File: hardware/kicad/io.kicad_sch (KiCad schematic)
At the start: 0 parts

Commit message: kicad+docs: v0.19 - IO sub-sheet populated (J9 Qwiic + J10 native-USB recovery DNP)
Closes review Mi4 ("IO sub-sheet still empty"). Implements both connectors
listed in CLAUDE.md as "tentative" since v0.1:

J9 - Qwiic / Stemma QT expansion (always populated)
  Stock JST_SH SM04B-SRSS-TB 4-pin horizontal SMD socket on cutout C5.
  Cable mouth faces the chord so the cable plugs in from outside the
  case. Pinout: GND / +3.3V / SDA / SCL — taps the shared I2C bus
  (SEN66 + NT3H1101 + Qwiic chain). I2C_SDA / I2C_SCL hier labels
  match the MCU exports.

J10 - Native-USB recovery header (DNP)
  Stock 6-pin 2.54 mm vertical THT pin header on cutout C3. Pads
  only — solder a header for emergency reflashing if both DevKitM-1
  on-module USB-C ports are damaged. Pinout (chord side → PCB
  interior): GND / +3V3 / USB_DM (GPIO 12) / USB_DP (GPIO 13) /
  EN (chip reset) / BOOT (GPIO 9 strap).

Cutout C4 reserved as v2 expansion placeholder (no connector).

Key plumbing changes:
  - GPIO 12 / GPIO 13 moved from ESP32C6_DEVKITM1_NC_PINS to
    ESP32C6_DEVKITM1_SIGNAL_PIN as USB_DM / USB_DP. MCU sheet now
    wires U3.28 / U3.29 east to hier labels.
  - EN / BOOT migrated from MCU sub-sheet local labels to hier
    labels so the same nets reach the IO sheet's J10.5 / J10.6.
    J2_PIN_MAP[5] "RST" -> "EN".
  - CUTOUTS extended with allow_pads bool; C3 and C5 flip the
    copper keepout zone's pads-not-allowed rule so connector pads
    can live inside the case-wall opening.
  - SUBSHEET_SIZE bumped to (38.1, 17.78) for 6 pins per edge.
  - Root sheet inter-sheet wires extended for I2C bus → IO + new
    routes for USB_DM/USB_DP/EN/BOOT (MCU right ↔ IO left).
  - _emit_stock_lib_footprint() factored out the parse-and-patch
    logic shared by gen_j1/j3/j4 footprint generators; gen_j9 and
    gen_j10 are thin wrappers around it.

DRC = 0, ERC = 0.

BOM impact: +1 SKU (JST SM04B-SRSS-TB, ~€0.50). J10 pin header is
DNP — 0 BOM lines for the production assembly.

Co-Authored-By: Clau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
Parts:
- added J10: 1x6 P2.54mm pin header — native USB recovery (DNP), symbol Connector_Generic:Conn_01x06
- added J9: JST SH SM04B-SRSS-TB (Qwiic / Stemma QT), symbol Connector_Generic:Conn_01x04
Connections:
- new net +3V3: J10.2 (Pin_2), J9.2 (Pin_2)
- new net BOOT: J10.6 (Pin_6)
- new net EN: J10.5 (Pin_5)
- new net GND: J10.1 (Pin_1), J9.1 (Pin_1)
- new net I2C_SCL: J9.4 (Pin_4)
- new net I2C_SDA: J9.3 (Pin_3)
- new net USB_DM: J10.3 (Pin_3)
- new net USB_DP: J10.4 (Pin_4)

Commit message: kicad+docs: v0.24 - fix v0.23 regressions (lib-qualify footprints + ERC strict)
Closes review iteration 2 findings (`_review-iteration-2-v0.23.md`):

1. Mn3 V3 regression — lib-qualify footprint back-fill.
   `_build_pcb_ref_to_footprint()` now lib-qualifies bare PCB-side
   Footprint property values via a new `BARE_FOOTPRINT_TO_LIB` table
   (12 entries) and asserts every returned value contains `:`. In
   parallel, the inline `gen_*_pcb_footprint` generators that emitted
   bare names now write fully-qualified `Lib:Name` strings directly
   (`Capacitor_SMD:C_0402_1005Metric`, `Package_TO_SOT_SMD:SOT-23`,
   `Inductor_SMD:L_APV_ANR5040`, `Fuse:Fuse_2920_7451Metric`,
   `Capacitor_THT:CP_Radial_D8.0mm_P3.50mm`, etc.). 15 ERC
   `footprint_link_issues` warnings → 0.

2. Mj2 — `regenerate.py` ERC strict mode. `kicad-cli sch erc` now
   invoked with `--severity-error --severity-warning
   --exit-code-violations`, mirroring DRC strictness. Verified by
   corrupting a schematic Footprint property and confirming abort.
   CLAUDE.md "PCB design workflow" §3 ("aborts on any error or
   warning") is now actually enforced for ERC, not just DRC.

3. C1 V4 — derived `.kicad_pcb` / `.kicad_sch` resynced with
   `generate.py`. The v0.23 commit shipped `generate.py` updates
   without regenerating the derived files; this commit brings them
   into sync via `python regenerate.py`.

4. Mj1 — CLAUDE.md v0.23 changelog entry added retroactively
   (had been missing). v0.24 entry added documenting this fix
   series + the ERC-strictness lesson.

5. `hardware/components/_review-iteration-2-v0.23.md` committed
   (previously untracked).

DRC = 0 violations / 0 warnings.
ERC = 0 violations / 0 warnings (now strict).
Determinism self-check passes (17 files bit-identical across two
consecutive `regenerate.py` runs).

Co-Authored-By: Claude Opus 4.7 (1M context) <noreply@anthropic.com>
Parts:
- J10: footprint (none) -> Connector_PinHeader_2.54mm:PinHeader_1x06_P2.54mm_Vertical
- J9: footprint (none) -> Connector_JST:JST_SH_SM04B-SRSS-TB_1x04-1MP_P1.00mm_Horizontal
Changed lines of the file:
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@@
         			)
         		)
-        		(property "Footprint" ""
+        		(property "Footprint" "Connector_JST:JST_SH_SM04B-SRSS-TB_1x04-1MP_P1.00mm_Horizontal"
         			(at 95.25 82.55 0)
         			(effects
@@
         			)
         		)
-        		(property "Footprint" ""
+        		(property "Footprint" "Connector_PinHeader_2.54mm:PinHeader_1x06_P2.54mm_Vertical"
         			(at 95.25 132.08 0)
         			(effects

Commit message: kicad+bom: v0.36 - swarm-audit fixes (4 CRITICAL + 3 IMPORTANT)
All 30-agent swarm audit findings from _swarm-audit-v0.35.md addressed.

CRITICAL fixes (would have caused board failure):
- C1 D1 TVS polarity: schematic angle 90→270 AND PCB rotation 0→180
  jointly land KiCad D_SMB pad 1 (cathode) on +24V VIN (was on GND).
  Net renamed Net-(D1-A2) → Net-(D1-A1) in oas_routes.py.
- C2 TPS62933 FB divider: schematic R2 44.2k→100k, R3 10k→30.9k for
  correct Vref=0.8V (was designed against wrong Vref=0.6V assumption).
  Vout = 0.8 × (1 + 100/30.9) = 3.39V (within ±3% of 3.3V target).
- C3 C7/C8 align: PCB-generator C7=22pF/C8=100nF (with swapped BST/SS
  roles) was contradicting the schematic C7=100nF BST + C8=47nF SS.
  Aligned PCB-generator to schematic (correct TPS62933 config).
- C4 Q1 substitution: PMV65XP (Vds=-20V) → AO3401A (LCSC C15127,
  Vds=-30V, same SOT-23 footprint). 8.9V margin over SMBJ24A 38.9V
  clamp. AO3401A drop-in: 1=G, 2=S, 3=D — no PCB layout change.

IMPORTANT fixes:
- I1 silk polarity markers: cathode bar on F.SilkS for D_SMA/D_SMB/
  D_SOD-323 (D1/D2/D3); "+" mark for CP_Radial (C1/C3/C4). Bar X
  computed from pad inner edge so silk clears mask opening by 0.25mm.
- I2 J10 cutout C3 north wall: +28.998 → +27.498 so pad 6 (BOOT)
  fully inside keepout (was 0.7mm outside).
- I3 J2/J10 DNP: (in_bom yes)→(in_bom no) when dnp flag is set.
- I7 D3 value text "500mW" → "200mW" matching BZT52C18S datasheet.

R1 value text aligned "100k" → "100k 1%" for consistent BOM grouping.

Verification: DRC=0, ERC=0, determinism PASS (17 files bit-identical),
Z-clearance PASS (76 footprints), preflight PASS, BOM=12 Basic + 11
Extended SMD + 8 THT (zero unmapped rows).

Co-Authored-By: Claude Opus 4.7 (1M context) <noreply@anthropic.com>
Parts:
- J10: now left out of the parts list
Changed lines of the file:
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@@
         		(unit 1)
         		(exclude_from_sim no)
-        		(in_bom yes)
+        		(in_bom no)
         		(on_board yes)
         		(dnp yes)

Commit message: kicad+bom: v0.38 - swarm audit v2 fixes (BOM-project coupling + silk polish)
30-agent read-only re-audit confirmed all v0.35-v0.37 CRITICAL fixes
in place and identified 6 follow-up items + 1 false positive. Applied
fixes:

Schematic ↔ BOM coupling (audit-16, primary user concern):
- generate.py: new _build_lcsc_metadata_map() + _apply_schematic_lcsc_metadata()
  injects Manufacturer / MPN / LCSC properties on every component symbol
  whose (Value, Footprint) matches a row in hardware/bom/lcsc-mapping.csv.
  Closes "projekt sobie, BOM sobie" — schematic is now self-sufficient
  for BOM export.
- export_production.py: BOM export switched to native kicad-cli --fields
  emitting Manufacturer + MPN columns directly from schematic. Post-process
  preserves them and adds JLCPCB_Library classification.
- New BOM CSV columns: Comment, Designator, Footprint, Manufacturer, MPN,
  LCSC, JLCPCB_Library, Qty.

Silkscreen polish (audit-26 / -27 / -24 / -28 / agent-08+11+30):
- D3 descriptor drift: 18V Zener → 10V Zener across generate.py PCB descr
  + 5 inline design comments (schematic Value + lcsc-mapping were already
  correct at v0.37; this fix syncs the source-of-truth comments).
- Radial cap "+" polarity marks: moved from pad_x+1.4 (INSIDE body radius,
  hidden post-assembly) to body_r+0.7 (~0.7 mm outside body, visible after
  the 8/6.3 mm cap solders down).
- SK6812 LED pin-1 dot: moved from F.Fab → F.SilkS in both lib generator
  and PCB-side footprint emitter, so the ring orientation is verifiable
  on physical PCB without consulting the assembly drawing.
- U1 LM2596S TO-263-5: added F.SilkS pin-1 dot at (-4.5, +1.5) radius 0.4
  for hand-assembly orientation.
- Board ID labels on F.SilkS: "Open Ambient Sensor" + "OAS v0.38" in the
  clear strip between MIKROE east edge (-12.7) and C3 cutout west (+4.9).
  Full repo URL on F.Fab (visible in renders, not silk-printed — URL too
  long for the strip at the 1.0 mm silk_min_text_height rule).

False positive confirmed (audit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
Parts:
- J9: LCSC (none) -> C160404; MPN (none) -> SM04B-SRSS-TB(LF)(SN); Manufacturer (none) -> JST Sales America
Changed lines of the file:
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@@
         			)
         		)
+		(property "Manufacturer" "JST Sales America"
+			(at 0 0 0)
+			(effects
+				(font
+					(size 1.27 1.27)
+				)
+				(hide yes)
+			)
+		)
+		(property "MPN" "SM04B-SRSS-TB(LF)(SN)"
+			(at 0 0 0)
+			(effects
+				(font
+					(size 1.27 1.27)
+				)
+				(hide yes)
+			)
+		)
+		(property "LCSC" "C160404"
+			(at 0 0 0)
+			(effects
+				(font
+					(size 1.27 1.27)
+				)
+				(hide yes)
+			)
+		)
         		(pin "1"
 		)

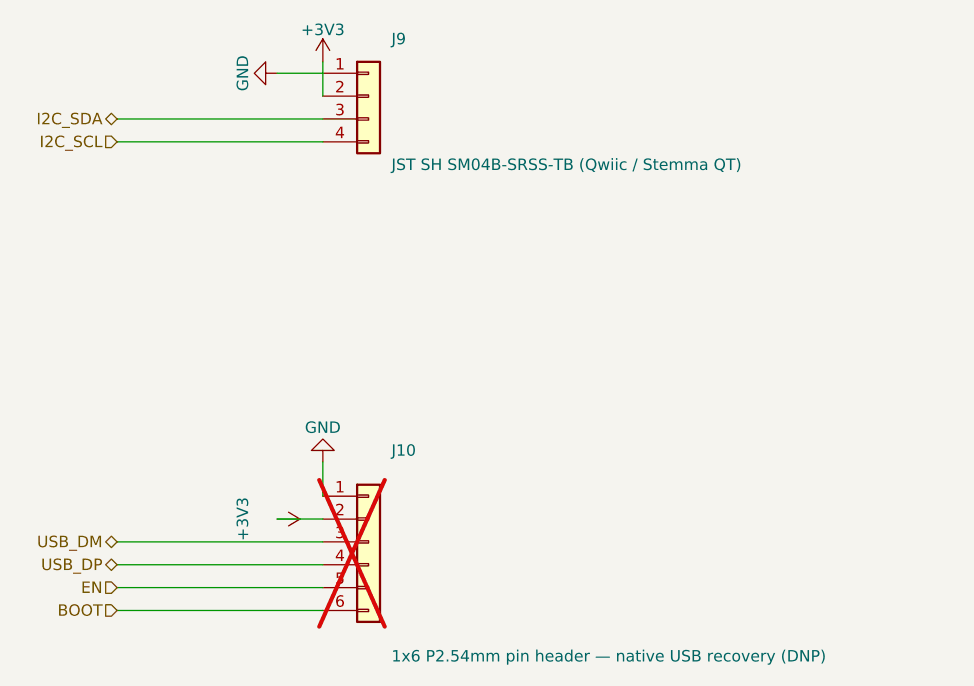
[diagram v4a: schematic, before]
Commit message: feat(sw1): add SW1 side-actuated tactile push-button (v0.42)
Adds the C&K PTS645VK392LFS right-angle THT push-button on ESP32-C6
GPIO 1, mounted in the AK-N-94 USB-C case-wall opening. Short press
cycles the LED ring brightness, long press restarts the MCU.

Hardware: GPIO 1 -> BTN net, new USBC cutout + SW1 placement constants,
Switch:SW_Push stock symbol on the IO sheet, verbatim-stock PTS645
footprint, inter-sheet BTN wiring (IO -> MCU). SW1 added to
THT_REFERENCES; DRC EXPECTED_UNCONNECTED 88 -> 89 (BTN ratsnest routed
in the pending routing rework).

Firmware: new packages/buttons.yaml (GPIO1 binary_sensor + brightness-
cycle script), wired into oas.yaml.

All 29 pipeline stages PASS; boardgen output deterministic.

Co-Authored-By: Claude Opus 4.7 <noreply@anthropic.com>
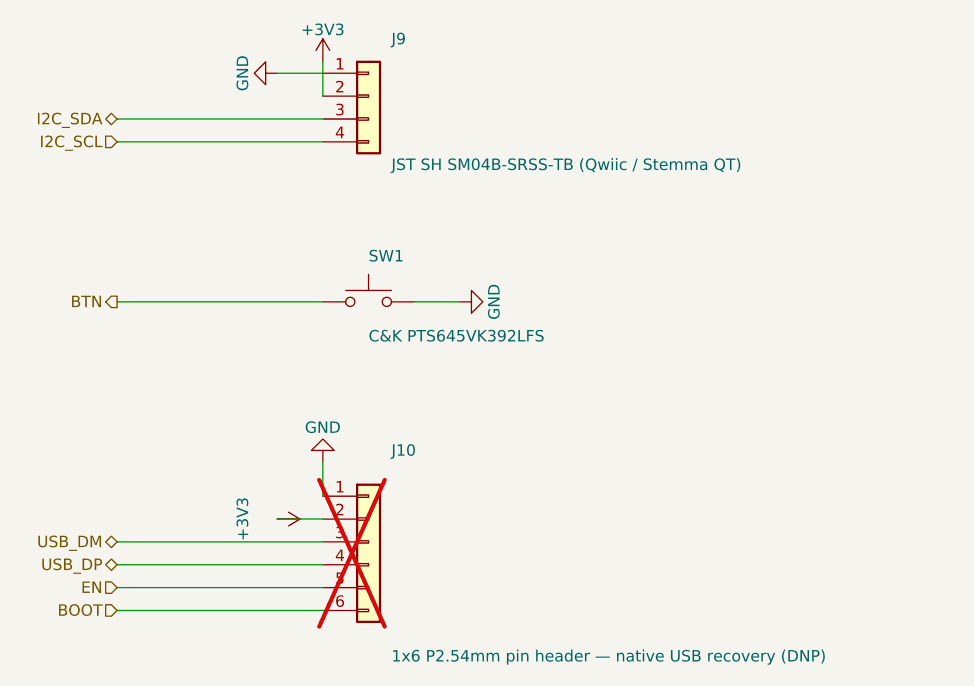
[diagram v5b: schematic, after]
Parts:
- added SW1: C&K PTS645VK392LFS, Button_Switch_THT:SW_Tactile_SPST_Angled_PTS645Vx39-2LFS, symbol Switch:SW_Push
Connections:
- net GND: now also SW1.2
- new net BTN: SW1.1
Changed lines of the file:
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@@
+	)
+)
+(wire
+	(pts
+		(xy 90.17 105.41) (xy 67.31 105.41)
+	)
+	(stroke
+		(width 0)
+		(type default)
+	)
+)
+(hierarchical_label "BTN"
+	(shape output)
+	(at 67.31 105.41 180)
+	(effects
+		(font
+			(size 1.27 1.27)
+		)
+		(justify right)
+	)
+)
+(wire
+	(pts
+		(xy 100.33 105.41) (xy 105.41 105.41)
+	)
+	(stroke
+		(width 0)
+		(type default)
+	)
+)
+(symbol
+	(lib_id "power:GND")
+	(at 105.41 105.41 90)
+	(unit 1)
+	(exclude_from_sim no)
+	(in_bom yes)
+	(on_board yes)
+	(dnp no)
+	(fields_autoplaced yes)
+	(property "Reference" "#PWR64"
+		(at 105.41 101.6 0)
+		(effects
+			(font
+				(size 1.27 1.27)
+			)
+			(hide yes)
+		)
+	)
+	(property "Value" "GND"
+		(at 109.22 105.41 0)
+		(effects
+			(font
+				(size 1.27 1.27)
+			)
+		)
+	)
+	(property "Footprint" ""
+		(at 105.41 105.41 0)
+		(effects
+			(font
+				(size 1.27 1.27)
+			)
+			(hide yes)
+		)
+	)
+	(property "Datasheet" ""
+		(at 105.41 105.41 0)
+		(effects
+			(font
+				(size 1.27 1.27)
+			)
+			(hide yes)
+		)
+	)
+	(property "Description" ""
+		(at 105.41 105.41 0)
+		(effects
+			(font
+				(size 1.27 1.27)
+			)
+			(hide yes)
+		)
+	)
+	(pin "1"
+	)
+	(instances
+		(project "oas"
+			(path "/515343fe-5590-5fd9-97ec-5bed0f979de2/30fc7086-1657-5b17-a13a-76780ee3d8bb"
+				(reference "#PWR64")
+				(unit 1)
+			)
+		)
 	)
 )
@@
         					(unit 1)
         				)
+        			)
+        		)
+        	)
+        	(symbol
+        		(lib_id "Switch:SW_Push")
+        		(at 95.25 105.41 0)
+        		(unit 1)
+        		(exclude_from_sim no)
+        		(in_bom yes)
+        		(on_board yes)
+        		(dnp no)
+        		(fields_autoplaced yes)
+        		(property "Reference" "SW1"
+        			(at 95.25 100.33 0)
+        			(effects
+        				(font
+        					(size 1.27 1.27)
+        				)
+        				(justify left)
+        			)
+        		)
+        		(property "Value" "C&K PTS645VK392LFS"
+        			(at 95.25 109.22 0)
+        			(effects
+        				(font
+        					(size 1.27 1.27)
+        				)
+        				(justify left)
+        			)
+        		)
+        		(property "Footprint" "Button_Switch_THT:SW_Tactile_SPST_Angled_PTS645Vx39-2LFS"
+        			(at 95.25 105.41 0)
+        			(effects
+        				(font
+        					(size 1.27 1.27)
+        				)
+        				(hide yes)
+        			)
+        		)
+        		(property "Datasheet" ""
+        			(at 95.25 105.41 0)
+        			(effects
+        				(font
+        					(size 1.27 1.27)
+        				)
+        				(hide yes)
+        			)
+        		)
+        		(property "Description" ""
+        			(at 95.25 105.41 0)
+        			(effects
+        				(font
+        					(size 1.27 1.27)
+        				)
+        				(hide yes)
+        			)
+        		)
+        		(pin "1"
+		)
+		(pin "2"
+		)
+        		(instances
+        			(project "oas"
+        				(path "/515343fe-5590-5fd9-97ec-5bed0f979de2/30fc7086-1657-5b17-a13a-76780ee3d8bb"
+        					(reference "SW1")
+        					(unit 1)
+        				)

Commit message: hardware+firmware: remove the SW1 user push-button
Closes #5.

- boardgen: drop SW1 (C&K PTS645VK392LFS) from the IO schematic sheet,
  PCB placement, footprint emitters and Z-clearance entries; GPIO1
  (J5.8) becomes a spare no_connect and joins GPIO_SPARE (9 spares).
  The AK-N-94 USB-C case-wall opening annotation stays (enclosure
  feature) but no longer hosts a component.
- routing snapshot: remove the 9 /IO/BTN records, canonical re-extract
  renumbers uuid_tags -> 606 segments + 40 vias (was 613 + 42);
  test_project_constants + test_extract_routes counts updated.
- pipeline: SW1 out of THT_REFERENCES and the silk-strip special cases.
- firmware: delete packages/buttons.yaml and its include from oas.yaml
  (7 -> 6 packages); README updated.
- docs: CLAUDE.md module list, GPIO pinout table, spare-GPIO list,
  THT hand-solder TODO, repo-layout package list.

build.py 35/35 PASS; DRC 0 violations / 0 unconnected; ERC 0/0.

Co-Authored-By: Claude Fable 5 <noreply@anthropic.com>
Claude-Session: https://claude.ai/code/session_017QqgHNrNySNTKB44F1FsEB
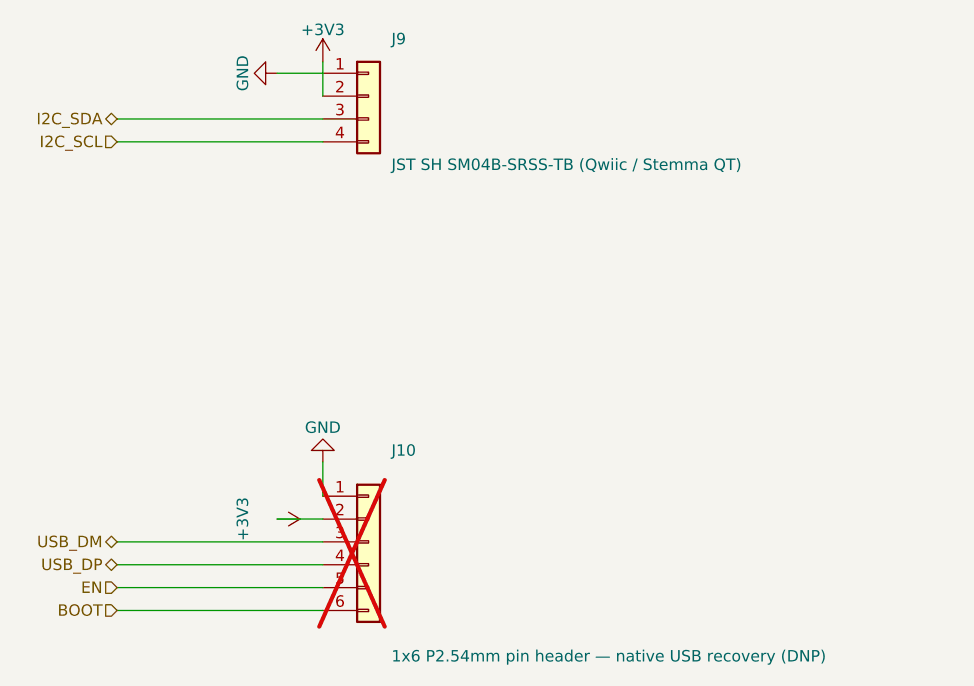
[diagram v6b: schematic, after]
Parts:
- removed SW1: C&K PTS645VK392LFS, Button_Switch_THT:SW_Tactile_SPST_Angled_PTS645Vx39-2LFS, symbol Switch:SW_Push
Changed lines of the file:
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@@
-	)
-)
-(wire
-	(pts
-		(xy 90.17 105.41) (xy 67.31 105.41)
-	)
-	(stroke
-		(width 0)
-		(type default)
-	)
-)
-(hierarchical_label "BTN"
-	(shape output)
-	(at 67.31 105.41 180)
-	(effects
-		(font
-			(size 1.27 1.27)
-		)
-		(justify right)
-	)
-)
-(wire
-	(pts
-		(xy 100.33 105.41) (xy 105.41 105.41)
-	)
-	(stroke
-		(width 0)
-		(type default)
-	)
-)
-(symbol
-	(lib_id "power:GND")
-	(at 105.41 105.41 90)
-	(unit 1)
-	(exclude_from_sim no)
-	(in_bom yes)
-	(on_board yes)
-	(dnp no)
-	(fields_autoplaced yes)
-	(property "Reference" "#PWR64"
-		(at 105.41 101.6 0)
-		(effects
-			(font
-				(size 1.27 1.27)
-			)
-			(hide yes)
-		)
-	)
-	(property "Value" "GND"
-		(at 109.22 105.41 0)
-		(effects
-			(font
-				(size 1.27 1.27)
-			)
-		)
-	)
-	(property "Footprint" ""
-		(at 105.41 105.41 0)
-		(effects
-			(font
-				(size 1.27 1.27)
-			)
-			(hide yes)
-		)
-	)
-	(property "Datasheet" ""
-		(at 105.41 105.41 0)
-		(effects
-			(font
-				(size 1.27 1.27)
-			)
-			(hide yes)
-		)
-	)
-	(property "Description" ""
-		(at 105.41 105.41 0)
-		(effects
-			(font
-				(size 1.27 1.27)
-			)
-			(hide yes)
-		)
-	)
-	(pin "1"
-	)
-	(instances
-		(project "oas"
-			(path "/515343fe-5590-5fd9-97ec-5bed0f979de2/30fc7086-1657-5b17-a13a-76780ee3d8bb"
-				(reference "#PWR64")
-				(unit 1)
-			)
-		)
 	)
 )
@@
         					(unit 1)
         				)
-        			)
-        		)
-        	)
-        	(symbol
-        		(lib_id "Switch:SW_Push")
-        		(at 95.25 105.41 0)
-        		(unit 1)
-        		(exclude_from_sim no)
-        		(in_bom yes)
-        		(on_board yes)
-        		(dnp no)
-        		(fields_autoplaced yes)
-        		(property "Reference" "SW1"
-        			(at 95.25 100.33 0)
-        			(effects
-        				(font
-        					(size 1.27 1.27)
-        				)
-        				(justify left)
-        			)
-        		)
-        		(property "Value" "C&K PTS645VK392LFS"
-        			(at 95.25 109.22 0)
-        			(effects
-        				(font
-        					(size 1.27 1.27)
-        				)
-        				(justify left)
-        			)
-        		)
-        		(property "Footprint" "Button_Switch_THT:SW_Tactile_SPST_Angled_PTS645Vx39-2LFS"
-        			(at 95.25 105.41 0)
-        			(effects
-        				(font
-        					(size 1.27 1.27)
-        				)
-        				(hide yes)
-        			)
-        		)
-        		(property "Datasheet" ""
-        			(at 95.25 105.41 0)
-        			(effects
-        				(font
-        					(size 1.27 1.27)
-        				)
-        				(hide yes)
-        			)
-        		)
-        		(property "Description" ""
-        			(at 95.25 105.41 0)
-        			(effects
-        				(font
-        					(size 1.27 1.27)
-        				)
-        				(hide yes)
-        			)
-        		)
-        		(pin "1"
-		)
-		(pin "2"
-		)
-        		(instances
-        			(project "oas"
-        				(path "/515343fe-5590-5fd9-97ec-5bed0f979de2/30fc7086-1657-5b17-a13a-76780ee3d8bb"
-        					(reference "SW1")
-        					(unit 1)
-        				)
